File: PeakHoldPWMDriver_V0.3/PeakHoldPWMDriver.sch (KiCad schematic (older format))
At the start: 117 parts, among them J1 RND 205-00203, J2 RND 205-00205, Q1 2N7002, Q10 2N7002, Q11 2N7002, Q12 2N7002, Q13 TSM2309, Q14 IRLL 024N, Q15 TSM2309, Q16 IRLL 024N, Q17 TSM2309, Q18 TSM2309, Q19 TSM2309, Q2 2N7002, Q20 TSM2309, Q3 2N7002, Q4 2N7002, Q5 TSM2309, Q6 TSM2309, Q7 IRLL 024N, Q8 IRLL 024N, Q9 2N7002, U1 74LS32, U2 LM2901, U3 74LS74, U4 LTC6992, U5 74LS74, U6 LM340, U7 74LS08, U8 74LS08

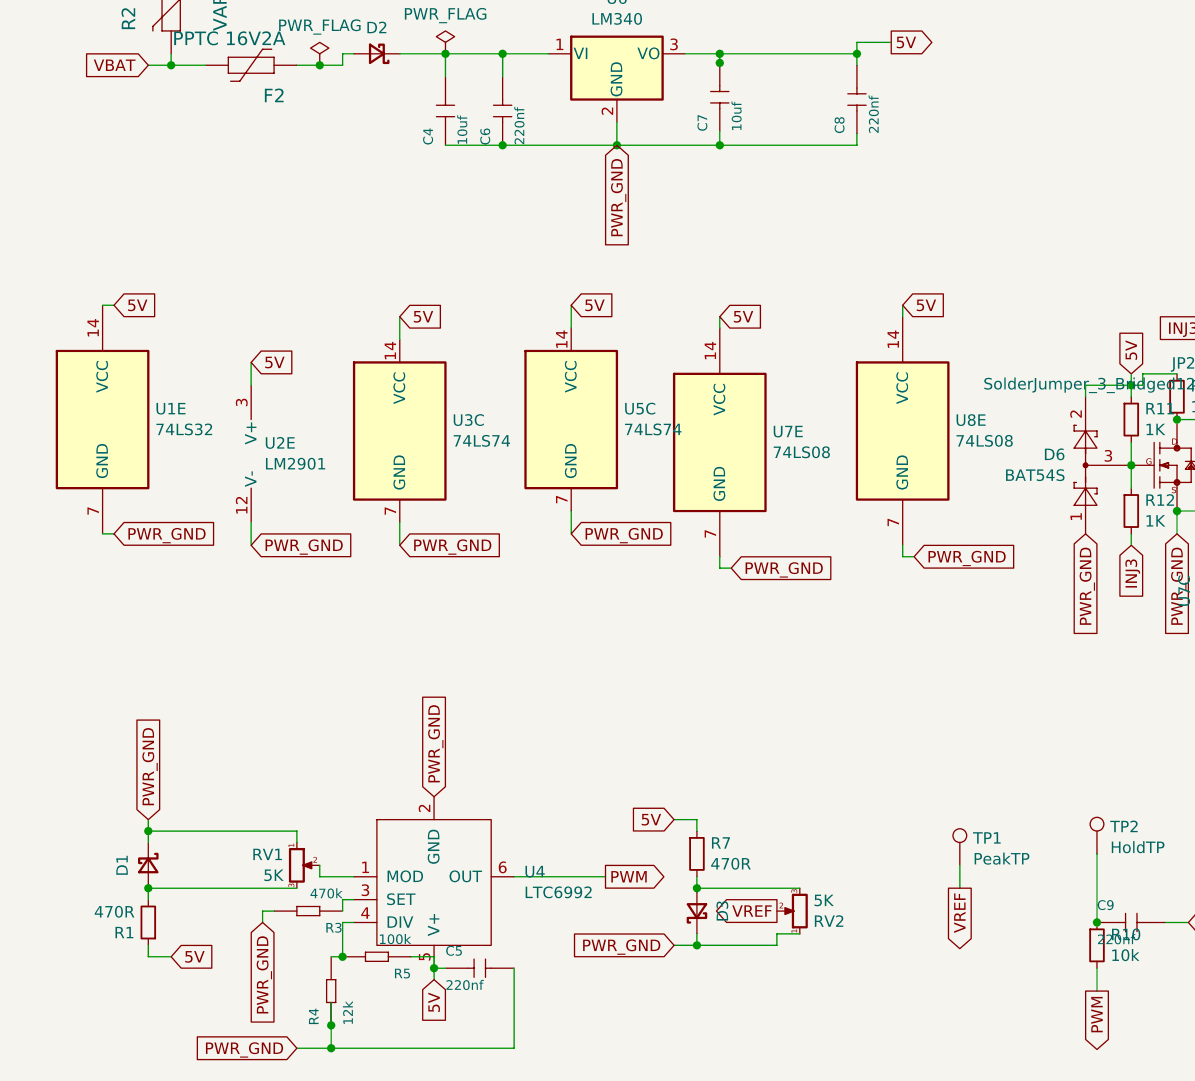
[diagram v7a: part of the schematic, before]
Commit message: PCB and schematic updated with battery voltage compensation
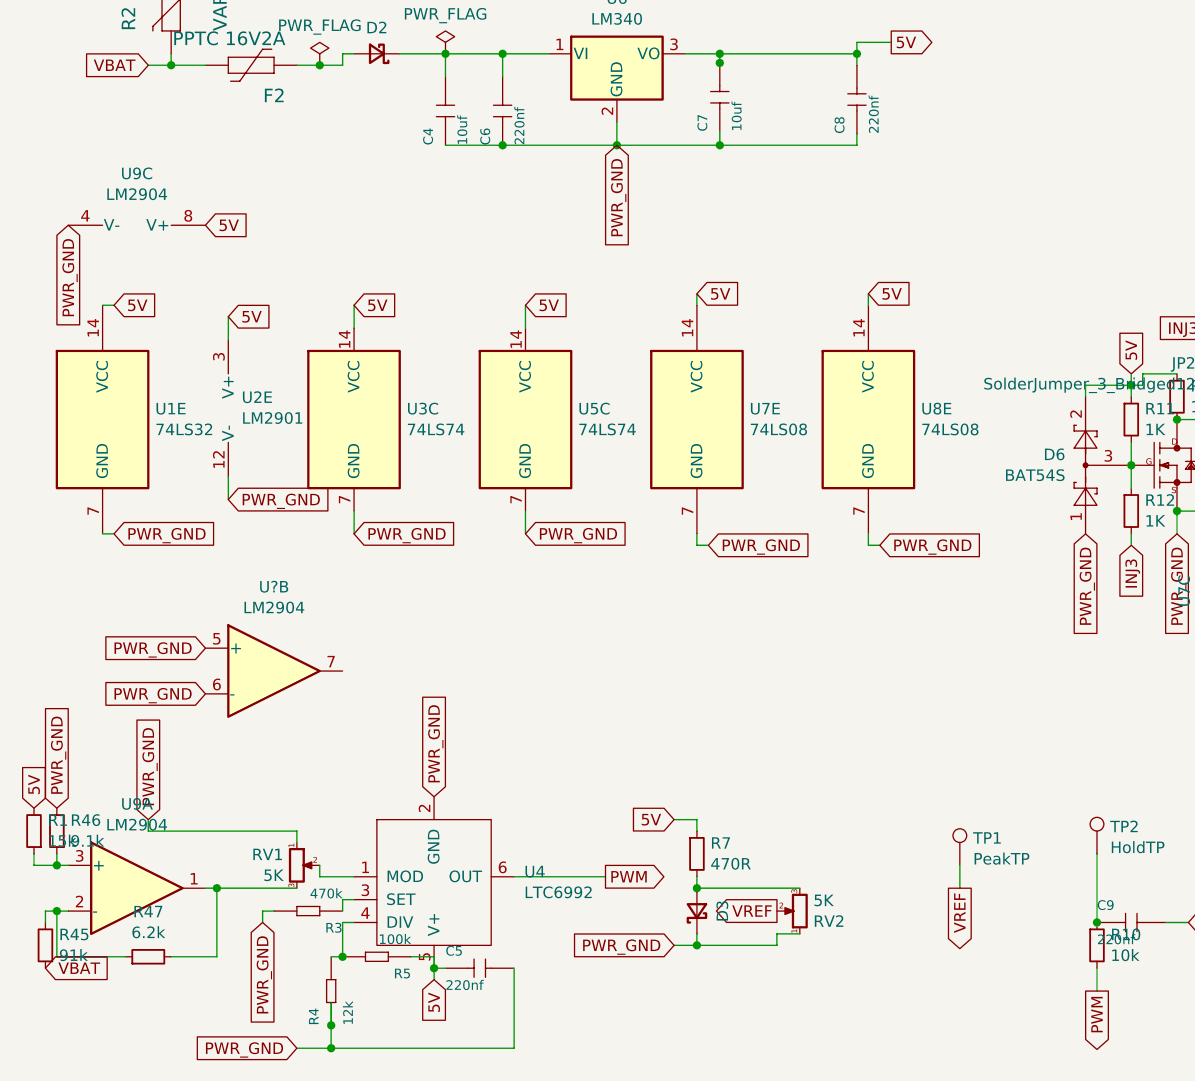
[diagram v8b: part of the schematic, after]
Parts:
- removed D1: BAV103, Diode_SMD:D_MiniMELF, symbol Device:D_Schottky_Small
- added R45: 91k, Resistor_SMD:R_0603_1608Metric, symbol Device:R_Small
- added R46: 9.1k, Resistor_SMD:R_0603_1608Metric, symbol Device:R_Small
- added R47: 6.2k, Resistor_SMD:R_0603_1608Metric, symbol Device:R_Small
- added U9, U?: LM2904, Package_SO:SO-8_3.9x4.9mm_P1.27mm, symbol Amplifier_Operational:LM2904
- R1: value 470R -> 15k; footprint Resistor_SMD:R_0603_1608Metric_Pad1.05x0.95mm_HandSolder -> Resistor_SMD:R_0603_1608Metric
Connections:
- net 5V: now also R1.2, U9.8 (V+); no longer R1.1
- net PWR_GND: now also R46.2, U9.4 (V-), U?.5 (+), U?.6 (-)
- net VBAT: now also R45.1
- net at RV1.3: now also R47.2, U9.1; no longer R1.2
- new net: R45.2, R47.1, U9.2 (-)
- new net: R1.1, R46.1, U9.3 (+)
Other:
- moved on the sheet: U2E, U3C, U5C, U7E, U8E
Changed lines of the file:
@@
 L Comparator:LM2901 U2
 U 5 1 5EDACEAF
-P 1600 4750
-F 0 "U2" H 1558 4796 50  0000 L CNN
-F 1 "LM2901" H 1558 4705 50  0000 L CNN
-F 2 "Package_SO:SO-14_5.3x10.2mm_P1.27mm" H 1550 4850 50  0001 C CNN
-F 3 "https://www.st.com/resource/en/datasheet/lm2901.pdf" H 1650 4950 50  0001 C CNN
-	5    1600 4750
+P 1500 4550
+F 0 "U2" H 1458 4596 50  0000 L CNN
+F 1 "LM2901" H 1458 4505 50  0000 L CNN
+F 2 "Package_SO:SO-14_5.3x10.2mm_P1.27mm" H 1450 4650 50  0001 C CNN
+F 3 "https://www.st.com/resource/en/datasheet/lm2901.pdf" H 1550 4750 50  0001 C CNN
+	5    1500 4550
 	1    0    0    -1
 $EndComp
@@
 L 74xx:74LS08 U7
 U 5 1 5F10F026
-P 3550 4700
-F 0 "U7" H 3780 4746 50  0000 L CNN
-F 1 "74LS08" H 3780 4655 50  0000 L CNN
-F 2 "Package_SO:SO-14_5.3x10.2mm_P1.27mm" H 3550 4700 50  0001 C CNN
-F 3 "http://www.ti.com/lit/gpn/sn74LS08" H 3550 4700 50  0001 C CNN
-	5    3550 4700
+P 3450 4600
+F 0 "U7" H 3680 4646 50  0000 L CNN
+F 1 "74LS08" H 3680 4555 50  0000 L CNN
+F 2 "Package_SO:SO-14_5.3x10.2mm_P1.27mm" H 3450 4600 50  0001 C CNN
+F 3 "http://www.ti.com/lit/gpn/sn74LS08" H 3450 4600 50  0001 C CNN
+	5    3450 4600
 	1    0    0    -1
 $EndComp
@@
 Text GLabel 2300 6250 1    50   Input ~ 0
 PWR_GND
-$Comp
-L Device:R_Small R1
-U 1 1 5F079FC0
-P 1050 6800
-F 0 "R1" H 1109 6846 50  0000 L CNN
-F 1 "470R" H 1109 6755 50  0000 L CNN
-F 2 "Resistor_SMD:R_0603_1608Metric_Pad1.05x0.95mm_HandSolder" H 1050 6800 50  0001 C CNN
-F 3 "~" H 1050 6800 50  0001 C CNN
-	1    1050 6800
-	-1   0    0    1
-$EndComp
-Wire Wire Line
-	1050 6700 1050 6650
-Text GLabel 1150 6950 2    50   Input ~ 0
-5V
-Wire Wire Line
-	1150 6950 1050 6950
-Wire Wire Line
-	1050 6950 1050 6900
 $Comp
 L Device:R_POT_Small RV1
@@
 Wire Wire Line
 	2300 7000 2300 7050
-Text GLabel 2150 4150 2    50   Input ~ 0
+Text GLabel 1950 4100 2    50   Input ~ 0
 5V
-Text GLabel 2150 5150 2    50   Input ~ 0
-PWR_GND
-Text GLabel 3550 4150 2    50   Input ~ 0
+Text GLabel 1950 5100 2    50   Input ~ 0
+PWR_GND
+Text GLabel 3450 4050 2    50   Input ~ 0
 5V
-Text GLabel 3600 5250 2    50   Input ~ 0
-PWR_GND
-Wire Wire Line
-	2150 4250 2150 4150
-Wire Wire Line
-	2150 5050 2150 5150
-Text GLabel 1500 5150 2    50   Input ~ 0
-PWR_GND
-Wire Wire Line
-	1500 4450 1500 4350
-Wire Wire Line
-	1500 5050 1500 5150
+Text GLabel 3500 5150 2    50   Input ~ 0
+PWR_GND
+Wire Wire Line
+	1950 4200 1950 4100
+Wire Wire Line
+	1950 5000 1950 5100
+Text GLabel 1400 4950 2    50   Input ~ 0
+PWR_GND
+Wire Wire Line
+	1400 4250 1400 4150
+Wire Wire Line
+	1400 4850 1400 4950
 Text GLabel 7500 5250 2    50   Input ~ 0
 5V
@@
 Wire Wire Line
 	10250 4200 10300 4200
-Text GLabel 1500 4350 2    50   Input ~ 0
+Text GLabel 1400 4150 2    50   Input ~ 0
 5V
-$Comp
-L Device:D_Schottky_Small D1
-U 1 1 5F079FBA
-P 1050 6550
-F 0 "D1" H 1050 6437 50  0000 C CNN
-F 1 "BAV103" V 1095 6618 50  0001 L CNN
-F 2 "Diode_SMD:D_MiniMELF" V 1050 6550 50  0001 C CNN
-F 3 "~" V 1050 6550 50  0001 C CNN
-	1    1050 6550
-	0    1    1    0
-$EndComp
 $Comp
 L 74xx:74LS32 U1
@@
 	850  4100 900  4100
 Wire Wire Line
-	3550 5200 3550 5250
-Wire Wire Line
-	3550 5250 3600 5250
-Wire Wire Line
-	3550 4200 3550 4150
-Text GLabel 2900 4100 2    50   Input ~ 0
+	3450 5100 3450 5150
+Wire Wire Line
+	3450 5150 3500 5150
+Wire Wire Line
+	3450 4100 3450 4050
+Text GLabel 2700 4100 2    50   Input ~ 0
 5V
-Text GLabel 2900 5100 2    50   Input ~ 0
-PWR_GND
-Wire Wire Line
-	2900 4200 2900 4100
-Wire Wire Line
-	2900 5000 2900 5100
+Text GLabel 2700 5100 2    50   Input ~ 0
+PWR_GND
+Wire Wire Line
+	2700 4200 2700 4100
+Wire Wire Line
+	2700 5000 2700 5100
 $Comp
 L 74xx:74LS08 U8
@@
 L 74xx:74HC74 U5
 U 3 1 619D29D1
-P 2900 4600
-F 0 "U5" H 3130 4646 50  0000 L CNN
-F 1 "74LS74" H 3130 4555 50  0000 L CNN
-F 2 "Package_SO:SO-14_5.3x10.2mm_P1.27mm" H 2900 4600 50  0001 C CNN
-F 3 "http://www.ti.com/lit/gpn/sn74LS08" H 2900 4600 50  0001 C CNN
-	3    2900 4600
+P 2700 4600
+F 0 "U5" H 2930 4646 50  0000 L CNN
+F 1 "74LS74" H 2930 4555 50  0000 L CNN
+F 2 "Package_SO:SO-14_5.3x10.2mm_P1.27mm" H 2700 4600 50  0001 C CNN
+F 3 "http://www.ti.com/lit/gpn/sn74LS08" H 2700 4600 50  0001 C CNN
+	3    2700 4600
 	1    0    0    -1
 $EndComp
@@
 L 74xx:74HC74 U3
 U 3 1 5F0F47CC
-P 2150 4650
-F 0 "U3" H 2380 4696 50  0000 L CNN
-F 1 "74LS74" H 2380 4605 50  0000 L CNN
-F 2 "Package_SO:SO-14_5.3x10.2mm_P1.27mm" H 2150 4650 50  0001 C CNN
-F 3 "http://www.ti.com/lit/gpn/sn74LS08" H 2150 4650 50  0001 C CNN
-	3    2150 4650
+P 1950 4600
+F 0 "U3" H 2180 4646 50  0000 L CNN
+F 1 "74LS74" H 2180 4555 50  0000 L CNN
+F 2 "Package_SO:SO-14_5.3x10.2mm_P1.27mm" H 1950 4600 50  0001 C CNN
+F 3 "http://www.ti.com/lit/gpn/sn74LS08" H 1950 4600 50  0001 C CNN
+	3    1950 4600
 	1    0    0    -1
 $EndComp
@@
 L 74xx:74LS08 U8
 U 5 1 61F18708
-P 4350 4650
-F 0 "U8" H 4580 4696 50  0000 L CNN
-F 1 "74LS08" H 4580 4605 50  0000 L CNN
-F 2 "Package_SO:SO-14_5.3x10.2mm_P1.27mm" H 4350 4650 50  0001 C CNN
-F 3 "http://www.ti.com/lit/gpn/sn74LS08" H 4350 4650 50  0001 C CNN
-	5    4350 4650
-	1    0    0    -1
-$EndComp
-Text GLabel 4350 4100 2    50   Input ~ 0
+P 4200 4600
+F 0 "U8" H 4430 4646 50  0000 L CNN
+F 1 "74LS08" H 4430 4555 50  0000 L CNN
+F 2 "Package_SO:SO-14_5.3x10.2mm_P1.27mm" H 4200 4600 50  0001 C CNN
+F 3 "http://www.ti.com/lit/gpn/sn74LS08" H 4200 4600 50  0001 C CNN
+	5    4200 4600
+	1    0    0    -1
+$EndComp
+Text GLabel 4200 4050 2    50   Input ~ 0
 5V
 Wire Wire Line
-	4350 5150 4350 5200
-Wire Wire Line
-	4350 5200 4400 5200
-Wire Wire Line
-	4350 4150 4350 4100
+	4200 5100 4200 5150
+Wire Wire Line
+	4200 5150 4250 5150
+Wire Wire Line
+	4200 4100 4200 4050
 Wire Wire Line
 	6250 4800 7150 4800
@@
 Text GLabel 1050 6350 1    50   Input ~ 0
 PWR_GND
-Text GLabel 4400 5200 2    50   Input ~ 0
+Text GLabel 4250 5150 2    50   Input ~ 0
 PWR_GND
 $Comp
@@
 Wire Wire Line
 	1700 6400 1700 6450
-Connection ~ 1050 6400
-Wire Wire Line
-	1050 6400 1050 6450
-Wire Wire Line
-	1050 6650 1700 6650
-Connection ~ 1050 6650
 $Comp
 L Diode:BZX84Cxx D8
@@
 Wire Wire Line
 	9950 4000 10000 4000
+$Comp
+L Amplifier_Operational:LM2904 U9
+U 1 1 5F317FCB
+P 1000 6650
+F 0 "U9" H 1000 7017 50  0000 C CNN
+F 1 "LM2904" H 1000 6926 50  0000 C CNN
+F 2 "Package_SO:SO-8_3.9x4.9mm_P1.27mm" H 1000 6650 50  0001 C CNN
+F 3 "http://www.ti.com/lit/ds/symlink/lm358.pdf" H 1000 6650 50  0001 C CNN
+	1    1000 6650
+	1    0    0    -1
+$EndComp
+$Comp
+L Amplifier_Operational:LM2904 U9
+U 3 1 5F319C5B
+P 1000 3850
+F 0 "U9" V 675 3850 50  0000 C CNN
+F 1 "LM2904" V 766 3850 50  0000 C CNN
+F 2 "Package_SO:SO-8_3.9x4.9mm_P1.27mm" H 1000 3850 50  0001 C CNN
+F 3 "http://www.ti.com/lit/ds/symlink/lm358.pdf" H 1000 3850 50  0001 C CNN
+	3    1000 3850
+	0    1    1    0
+$EndComp
+Text GLabel 1300 3750 2    50   Input ~ 0
+5V
+Text GLabel 700  3750 3    50   Input ~ 0
+PWR_GND
+$Comp
+L Device:R_Small R45
+U 1 1 5F4D3115
+P 600 6900
+F 0 "R45" H 541 6854 50  0000 R CNN
+F 1 "91k" H 541 6945 50  0000 R CNN
+F 2 "Resistor_SMD:R_0603_1608Metric" H 600 6900 50  0001 C CNN
+F 3 "~" H 600 6900 50  0001 C CNN
+	1    600  6900
+	-1   0    0    1
+$EndComp
+$Comp
+L Device:R_Small R47
+U 1 1 5F4E267C
+P 1050 6950
+F 0 "R47" V 1246 6950 50  0000 C CNN
+F 1 "6.2k" V 1155 6950 50  0000 C CNN
+F 2 "Resistor_SMD:R_0603_1608Metric" H 1050 6950 50  0001 C CNN
+F 3 "~" H 1050 6950 50  0001 C CNN
+	1    1050 6950
+	0    -1   -1   0
+$EndComp
+Wire Wire Line
+	1150 6950 1350 6950
+Wire Wire Line
+	1350 6950 1350 6650
+Wire Wire Line
+	1300 6650 1350 6650
+Connection ~ 1350 6650
+Wire Wire Line
+	1350 6650 1700 6650
+Wire Wire Line
+	650  6950 650  6750
+Wire Wire Line
+	650  6750 700  6750
+Wire Wire Line
+	650  6950 950  6950
+Wire Wire Line
+	650  6750 600  6750
+Wire Wire Line
+	600  6750 600  6800
+Connection ~ 650  6750
+Text GLabel 600  7000 2    50   Input ~ 0
+VBAT
+$Comp
+L Device:R_Small R1
+U 1 1 5F55F3EA
+P 550 6400
+F 0 "R1" H 491 6354 50  0000 R CNN
+F 1 "15k" H 491 6445 50  0000 R CNN
+F 2 "Resistor_SMD:R_0603_1608Metric" H 550 6400 50  0001 C CNN
+F 3 "~" H 550 6400 50  0001 C CNN
+	1    550  6400
+	-1   0    0    1
+$EndComp
+$Comp
+L Device:R_Small R46
+U 1 1 5F5A7792
+P 650 6400
+F 0 "R46" H 591 6354 50  0000 R CNN
+F 1 "9.1k" H 591 6445 50  0000 R CNN
+F 2 "Resistor_SMD:R_0603_1608Metric" H 650 6400 50  0001 C CNN
+F 3 "~" H 650 6400 50  0001 C CNN
+	1    650  6400
+	-1   0    0    1
+$EndComp
+Text GLabel 550  6300 1    50   Input ~ 0
+5V
+Text GLabel 650  6300 1    50   Input ~ 0
+PWR_GND
+Wire Wire Line
+	550  6500 550  6550
+Wire Wire Line
+	550  6550 650  6550
+Wire Wire Line
+	650  6500 650  6550
+Connection ~ 650  6550
+Wire Wire Line
+	650  6550 700  6550
+$Comp
+L Amplifier_Operational:LM2904 U?
+U 2 1 5F7AED14
+P 1600 5700
+F 0 "U?" H 1600 6067 50  0000 C CNN
+F 1 "LM2904" H 1600 5976 50  0000 C CNN
+F 2 "Package_SO:SO-8_3.9x4.9mm_P1.27mm" H 1600 5700 50  0001 C CNN
+F 3 "http://www.ti.com/lit/ds/symlink/lm358.pdf" H 1600 5700 50  0001 C CNN
+	2    1600 5700
+	1    0    0    -1
+$EndComp
+Text GLabel 1300 5600 0    50   Input ~ 0
+PWR_GND
+Text GLabel 1300 5800 0    50   Input ~ 0
+PWR_GND
 $EndSCHEMATC
